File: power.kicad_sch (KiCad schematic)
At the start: 128 parts, among them Q2 BC817-25W, Q3 DZDH0401DW, Q4 DZDH0401DW, Q5 SI7613DN-T1-GE3, Q6 SI7613DN-T1-GE3, U1 LT8350RV, U2 MP2386GG, U3 TPS65983BAZBHR

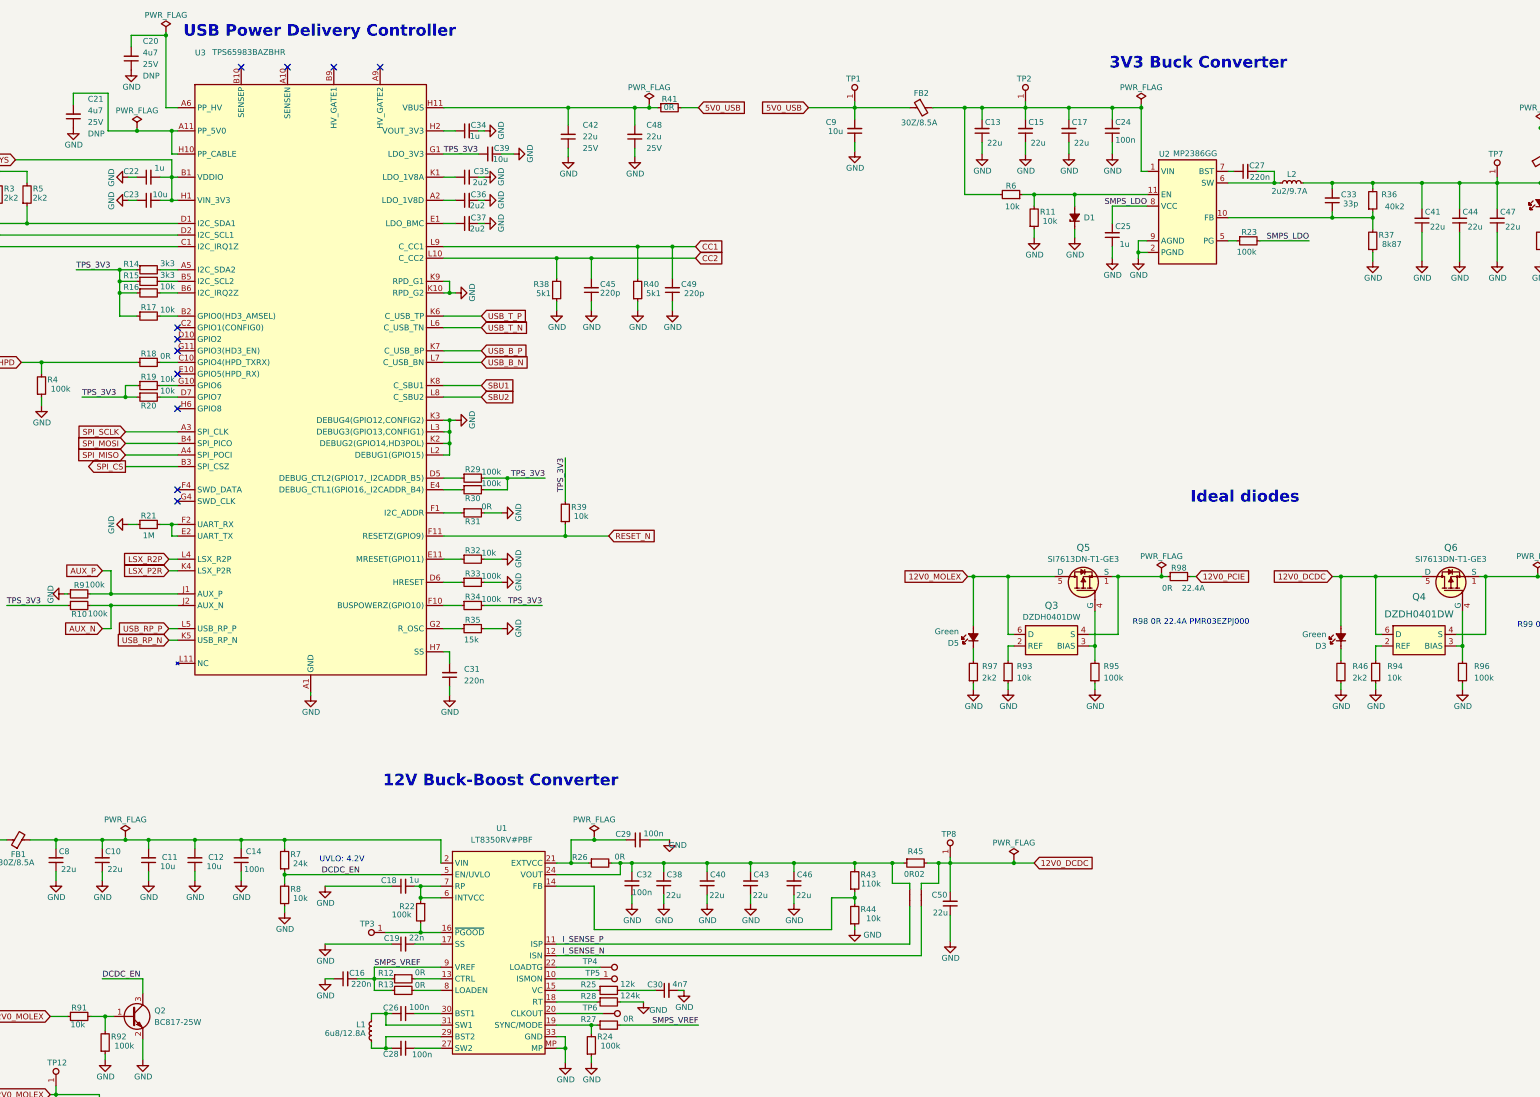
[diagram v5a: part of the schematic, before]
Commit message: [#58582] Clean ERC
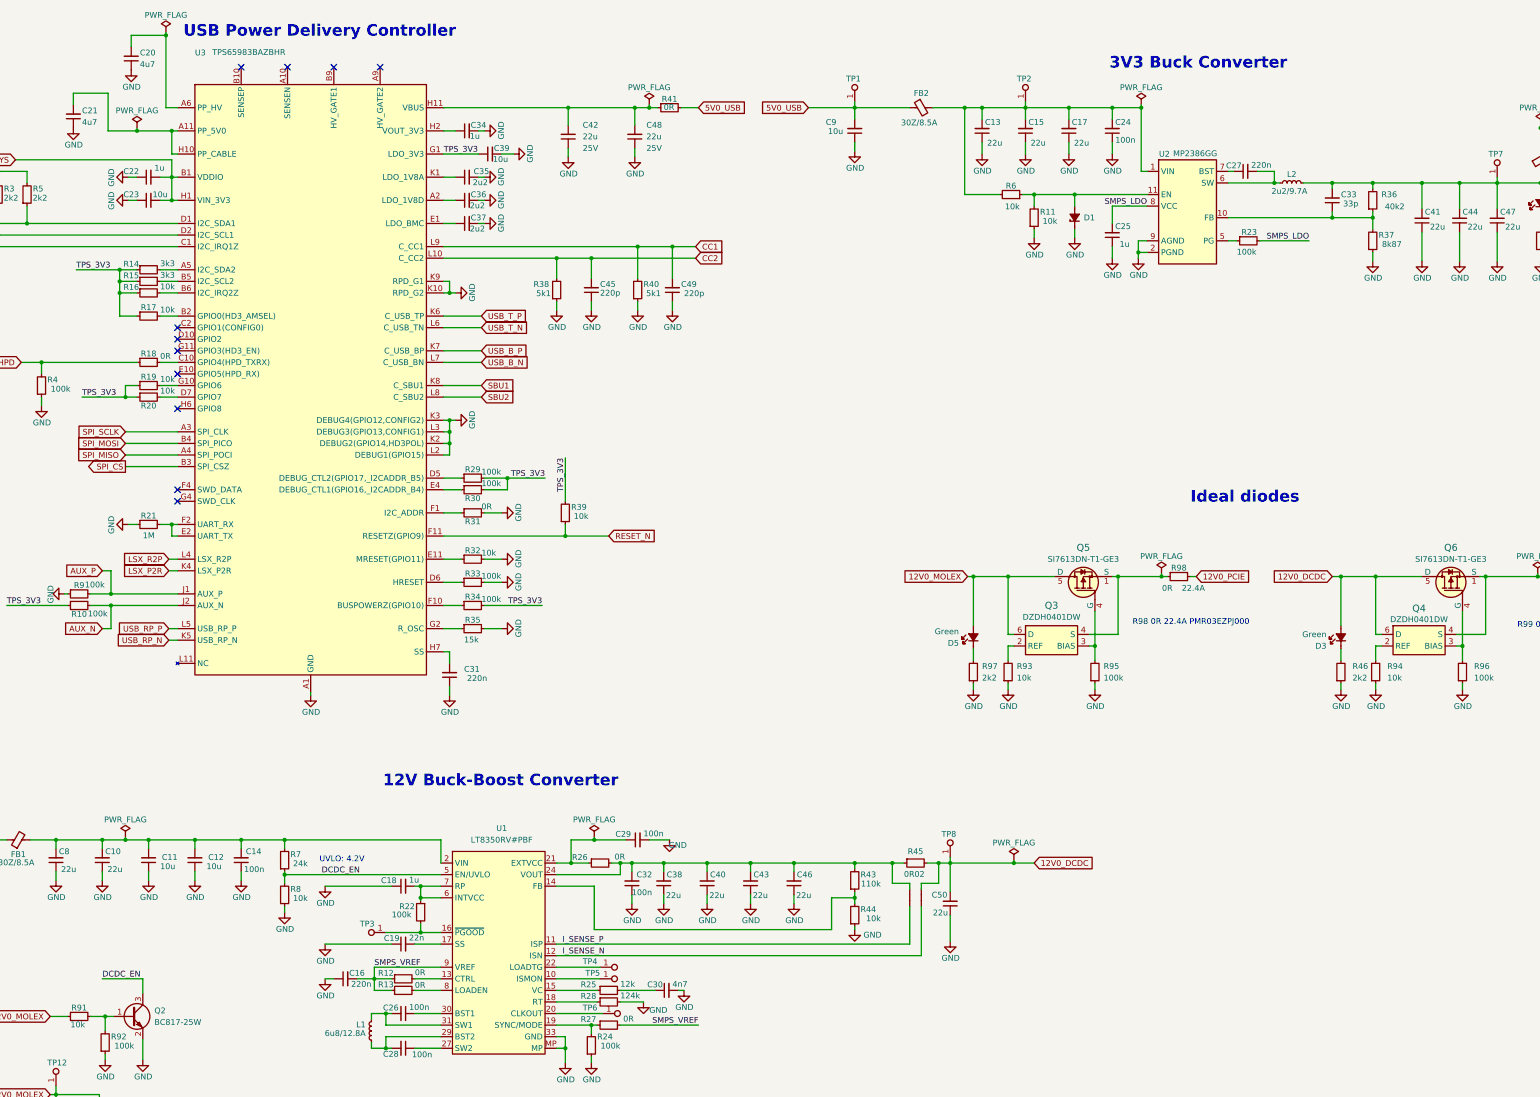
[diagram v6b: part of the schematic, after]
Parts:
- C20, C21: DNP DNP -> (none)
- C27, C31: Manufacturer Yaego -> YAGEO
- Q4: MPN DZDH0401DW-7 -> DZDH0401DW
- TP4, TP6: now left out of the parts list

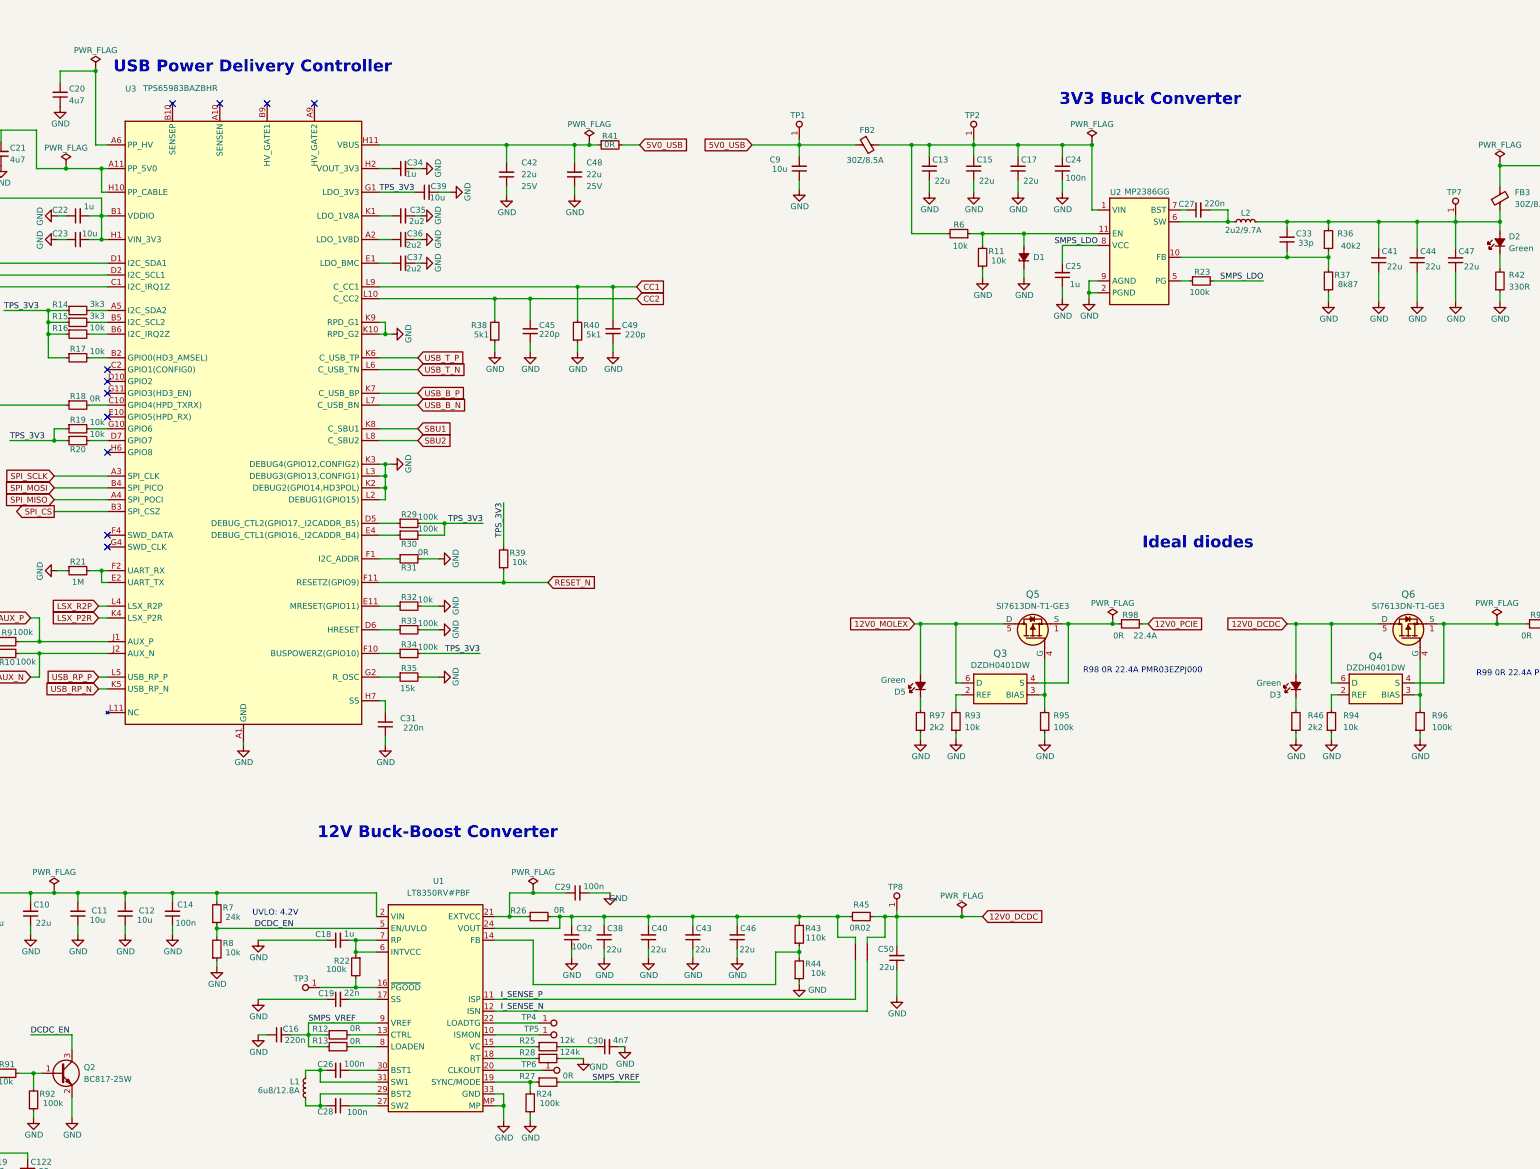
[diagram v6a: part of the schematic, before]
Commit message: [#58582] Update symbols values visibility
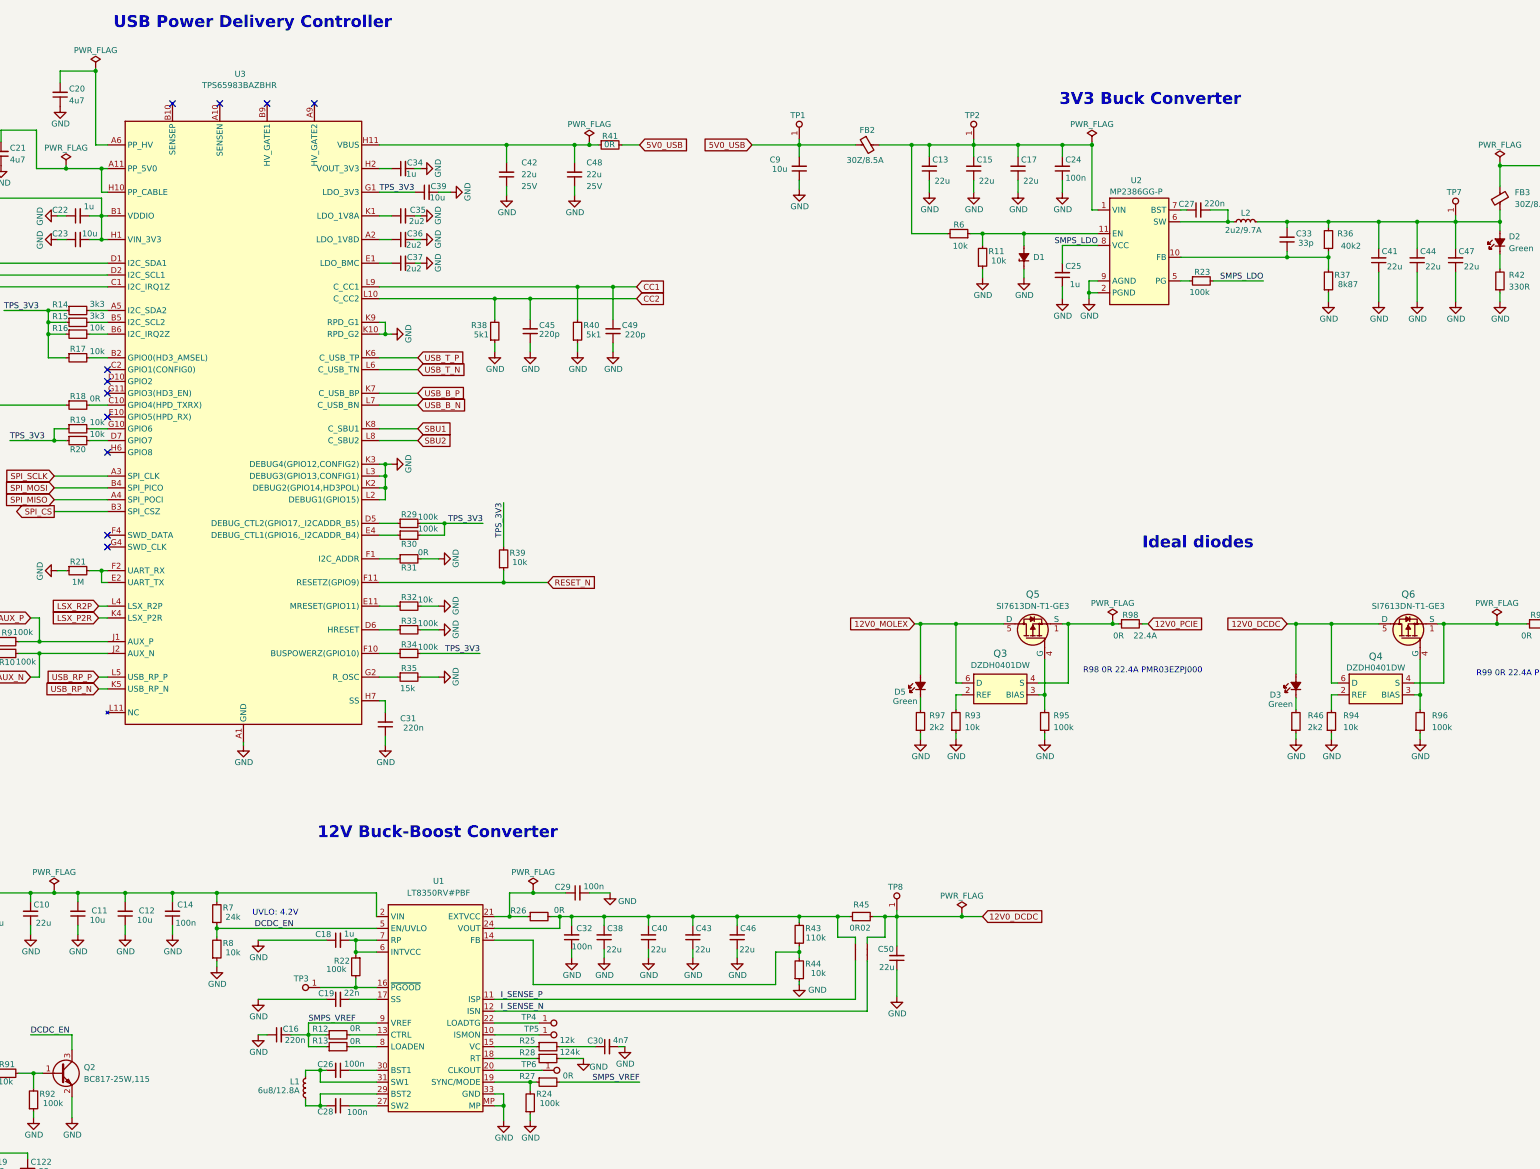
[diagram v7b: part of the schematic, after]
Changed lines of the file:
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@@
     (effects (font (size 2.54 2.54) bold) (justify left bottom))
   )
-  (text "USB Power Delivery Controller" (at 77.47 27.94 0)
+  (text "USB Power Delivery Controller" (at 77.47 18.415 0)
     (effects (font (size 2.54 2.54) bold) (justify left bottom))
   )
@@
       (effects (font (size 1.27 1.27)) hide)
     )
-    (property "Value" "GND" (at 187.96 205.74 0)
+    (property "Value" "GND" (at 189.865 206.375 0)
       (effects (font (size 1.27 1.27) (thickness 0.15)) (justify left bottom))
     )
@@
   (symbol (lib_id "antmicroDCDCConverters:MP2386GG") (at 288.925 57.15 0) (unit 1)
     (in_bom yes) (on_board yes) (dnp no)
-    (property "Reference" "U2" (at 292.735 53.34 0)
+    (property "Reference" "U2" (at 297.18 50.8 0)
       (effects (font (size 1.27 1.27) (thickness 0.15)))
     )
-    (property "Value" "MP2386GG" (at 294.64 53.975 0)
-      (effects (font (size 1.27 1.27) (thickness 0.15)) (justify left bottom))
+    (property "Value" "MP2386GG" (at 321.945 64.77 0)
+      (effects (font (size 1.27 1.27) (thickness 0.15)) (justify left bottom) hide)
     )
     (property "Footprint" "antmicro-footprints:QFN-11_2x2mm_P0.5mm" (at 321.945 67.31 0)
@@
       (effects (font (size 1.27 1.27) (thickness 0.15)) (justify left bottom) hide)
     )
-    (property "MPN" "MP2386GG-P" (at 321.945 74.93 0)
-      (effects (font (size 1.27 1.27) (thickness 0.15)) (justify left bottom) hide)
+    (property "MPN" "MP2386GG-P" (at 291.465 53.975 0)
+      (effects (font (size 1.27 1.27) (thickness 0.15)) (justify left bottom))
     )
     (property "License" "Apache-2.0" (at 321.945 80.01 0)
@@
       (effects (font (size 1.27 1.27) (thickness 0.15)) (justify left bottom) hide)
     )
-    (property "Color" "Green" (at 328.295 158.75 90)
-      (effects (font (size 1.27 1.27)) (justify left))
+    (property "Color" "Green" (at 330.835 162.56 90)
+      (effects (font (size 1.27 1.27)) (justify left bottom))
     )
     (pin "1")
@@
       (effects (font (size 1.524 1.524)))
     )
-    (property "Value" "DZDH0401DW" (at 267.97 154.94 0)
-      (effects (font (size 1.27 1.27) (thickness 0.15)))
+    (property "Value" "DZDH0401DW" (at 290.195 166.37 0)
+      (effects (font (size 1.27 1.27) (thickness 0.15)) (justify left bottom) hide)
     )
     (property "Footprint" "antmicro-footprints:SOT-363" (at 290.195 168.91 0)
@@
       (effects (font (size 1.27 1.27) (thickness 0.15)) (justify left bottom) hide)
     )
-    (property "MPN" "DZDH0401DW" (at 290.195 173.99 0)
-      (effects (font (size 1.27 1.27) (thickness 0.15)) (justify left bottom) hide)
+    (property "MPN" "DZDH0401DW" (at 267.97 154.94 0)
+      (effects (font (size 1.27 1.27) (thickness 0.15)))
     )
     (property "Manufacturer" "Diodes Incorporated" (at 290.195 176.53 0)
@@
       (effects (font (size 1.27 1.27) (thickness 0.15)) (justify left))
     )
-    (property "Value" "BC817-25W" (at 71.12 243.84 0)
-      (effects (font (size 1.27 1.27) (thickness 0.15)) (justify left))
+    (property "Value" "BC817-25W" (at 85.09 245.11 0)
+      (effects (font (size 1.27 1.27) (thickness 0.15)) (justify left bottom) hide)
     )
     (property "Footprint" "antmicro-footprints:SOT-323" (at 85.09 247.65 0)
@@
       (effects (font (size 1.27 1.27) (thickness 0.15)) (justify left bottom) hide)
     )
-    (property "MPN" "BC817-25W,115" (at 85.09 252.73 0)
-      (effects (font (size 1.27 1.27) (thickness 0.15)) (justify left bottom) hide)
+    (property "MPN" "BC817-25W,115" (at 71.12 243.84 0)
+      (effects (font (size 1.27 1.27) (thickness 0.15)) (justify left))
     )
     (property "Manufacturer" "Nexperia" (at 85.09 255.27 0)
@@
       (effects (font (size 1.524 1.524)))
     )
-    (property "Value" "SI7613DN-T1-GE3" (at 274.955 142.24 90)
-      (effects (font (size 1.27 1.27) (thickness 0.15)))
+    (property "Value" "SI7613DN-T1-GE3" (at 274.955 138.43 0)
+      (effects (font (size 1.27 1.27) (thickness 0.15)) (justify left bottom) hide)
     )
     (property "Footprint" "antmicro-footprints:Vishay_PowerPAK_1212-8_Single" (at 276.225 138.43 0)
@@
       (effects (font (size 1.27 1.27) (thickness 0.15)) (justify left bottom) hide)
     )
-    (property "MPN" "SI7613DN-T1-GE3" (at 282.575 138.43 0)
-      (effects (font (size 1.27 1.27) (thickness 0.15)) (justify left bottom) hide)
+    (property "MPN" "SI7613DN-T1-GE3" (at 274.955 142.24 90)
+      (effects (font (size 1.27 1.27) (thickness 0.15)))
     )
     (property "Manufacturer" "Vishay" (at 285.115 138.43 0)
@@
       (effects (font (size 1.27 1.27) (thickness 0.15)) (justify left bottom) hide)
     )
-    (property "Color" "Green" (at 247.65 158.115 90)
-      (effects (font (size 1.27 1.27)) (justify left))
+    (property "Color" "Green" (at 250.19 161.925 90)
+      (effects (font (size 1.27 1.27)) (justify left bottom))
     )
     (pin "1")
@@
   (symbol (lib_id "antmicroInterfaceControllers:TPS65983BAZBHR") (at 76.2 43.18 0) (unit 1)
     (in_bom yes) (on_board yes) (dnp no)
-    (property "Reference" "U3" (at 80.01 31.115 0)
+    (property "Reference" "U3" (at 103.505 27.94 0)
       (effects (font (size 1.27 1.27) (thickness 0.15)) (justify left))
     )
-    (property "Value" "TPS65983BAZBHR" (at 83.82 31.75 0)
-      (effects (font (size 1.27 1.27) (thickness 0.15)) (justify left bottom))
+    (property "Value" "TPS65983BAZBHR" (at 149.86 43.18 0)
+      (effects (font (size 1.27 1.27) (thickness 0.15)) (justify left bottom) hide)
     )
     (property "Footprint" "antmicro-footprints:IC_TPS65983BAZBHR" (at 149.86 45.72 0)
@@
       (effects (font (size 1.27 1.27) (thickness 0.15)) (justify left bottom) hide)
     )
-    (property "MPN" "TPS65983BAZBHR" (at 149.86 50.8 0)
-      (effects (font (size 1.27 1.27) (thickness 0.15)) (justify left bottom) hide)
+    (property "MPN" "TPS65983BAZBHR" (at 96.52 31.115 0)
+      (effects (font (size 1.27 1.27) (thickness 0.15)) (justify left bottom))
     )
     (property "Manufacturer" "Texas Instruments" (at 149.86 53.34 0)
@@
       (effects (font (size 1.524 1.524)))
     )
-    (property "Value" "SI7613DN-T1-GE3" (at 355.6 142.24 90)
-      (effects (font (size 1.27 1.27) (thickness 0.15)))
+    (property "Value" "SI7613DN-T1-GE3" (at 355.6 138.43 0)
+      (effects (font (size 1.27 1.27) (thickness 0.15)) (justify left bottom) hide)
     )
     (property "Footprint" "antmicro-footprints:Vishay_PowerPAK_1212-8_Single" (at 356.87 138.43 0)
@@
       (effects (font (size 1.27 1.27) (thickness 0.15)) (justify left bottom) hide)
     )
-    (property "MPN" "SI7613DN-T1-GE3" (at 363.22 138.43 0)
-      (effects (font (size 1.27 1.27) (thickness 0.15)) (justify left bottom) hide)
+    (property "MPN" "SI7613DN-T1-GE3" (at 355.6 142.24 90)
+      (effects (font (size 1.27 1.27) (thickness 0.15)))
     )
     (property "Manufacturer" "Vishay" (at 365.76 138.43 0)
@@
       (effects (font (size 1.524 1.524)))
     )
-    (property "Value" "DZDH0401DW" (at 342.265 156.21 0)
-      (effects (font (size 1.27 1.27) (thickness 0.15)) (justify left bottom))
-    )
-    (property "Footprint" "antmicro-footprints:SOT-363" (at 345.44 153.67 0)
+    (property "Value" "DZDH0401DW" (at 370.84 166.37 0)
       (effects (font (size 1.27 1.27) (thickness 0.15)) (justify left bottom) hide)
     )
-    (property "Datasheet" "https://www.mouser.com/datasheet/2/115/DIOD_S_A0011803041_1-2543705.pdf" (at 345.44 151.13 0)
+    (property "Footprint" "antmicro-footprints:SOT-363" (at 370.84 168.91 0)
       (effects (font (size 1.27 1.27) (thickness 0.15)) (justify left bottom) hide)
     )
-    (property "MPN" "DZDH0401DW" (at 345.44 151.13 0)
+    (property "Datasheet" "https://www.mouser.com/datasheet/2/115/DIOD_S_A0011803041_1-2543705.pdf" (at 370.84 171.45 0)
       (effects (font (size 1.27 1.27) (thickness 0.15)) (justify left bottom) hide)
     )
-    (property "Manufacturer" "Diodes Incorporated" (at 345.44 148.59 0)
+    (property "MPN" "DZDH0401DW" (at 342.265 156.21 0)
+      (effects (font (size 1.27 1.27) (thickness 0.15)) (justify left bottom))
+    )
+    (property "Manufacturer" "Diodes Incorporated" (at 370.84 176.53 0)
       (effects (font (size 1.27 1.27) (thickness 0.15)) (justify left bottom) hide)
     )
